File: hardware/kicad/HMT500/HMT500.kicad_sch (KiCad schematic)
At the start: 0 parts

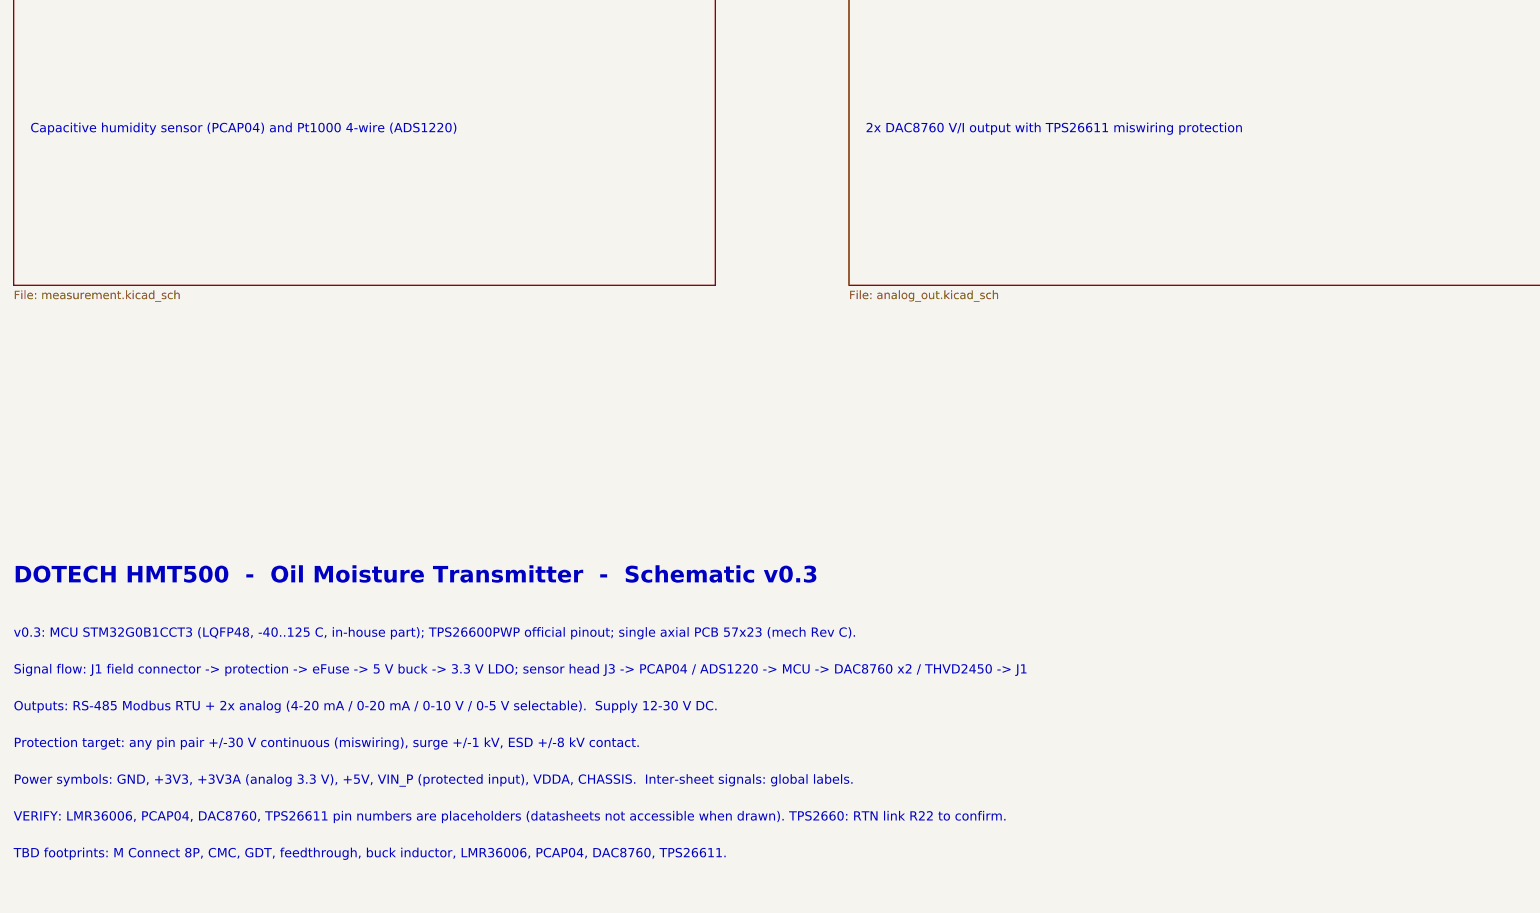
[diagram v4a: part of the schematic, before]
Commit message: Sensor harness W-1: JST SH 1.0 mm 4P between feedthrough and PCB J3
- Schematic v0.4: J3 = BM04B-SRSS-TB (top entry). Pins 1-2 MK33, 3-4 Pt1000
  2-wire with force/sense split at the J3 pads (68 nets, netlist check 0 errors)
- Parts list: J3 header, SHR-04V-S housing, SSH-003T-P0.2-H contacts, PTFE AWG30 wire
- Mech: J3 and harness in params/CAD/drawings (item 17, notes 5 and 9), PCAP04
  moved directly behind J3, PCB outline and KiCad board zone updated
- Test for harness clearance, J3 height and pin mapping
- Decision log #16; JST SH -25..+85 C rating added to open items

Co-Authored-By: Claude Opus 5.5 <noreply@anthropic.com>
Claude-Session: https://claude.ai/code/session_01JA2o8uJsqp9Vzsg4b665ev
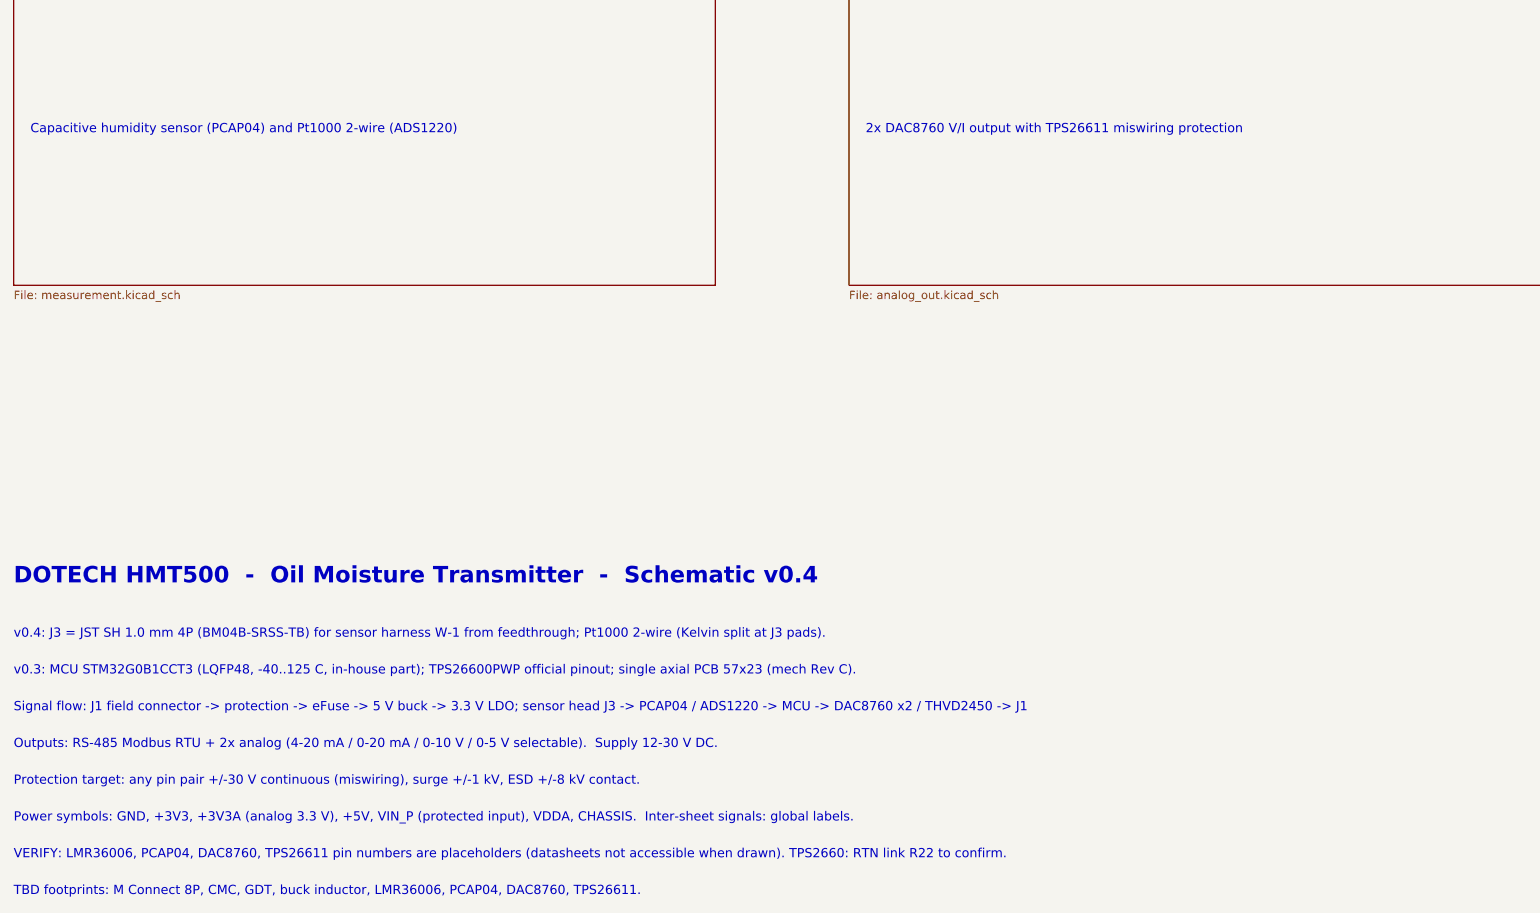
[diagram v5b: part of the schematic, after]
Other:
- note added: "Capacitive humidity sensor (PCAP04) and Pt1000 2-wire (ADS1220)"
- note added: "DOTECH HMT500 - Oil Moisture Transmitter - Schematic v0.4"
- note added: "TBD footprints: M Connect 8P, CMC, GDT, buck inductor, LMR36006, PCAP04, DAC8760, TPS26611."
- note added: "v0.4: J3 = JST SH 1.0 mm 4P (BM04B-SRSS-TB) for sensor harness W-1 from feedthrough; Pt1000 2-wire (Kelvin split at J3 pads)."
- note removed: "Capacitive humidity sensor (PCAP04) and Pt1000 4-wire (ADS1220)"
- note removed: "DOTECH HMT500 - Oil Moisture Transmitter - Schematic v0.3"
- note removed: "TBD footprints: M Connect 8P, CMC, GDT, feedthrough, buck inductor, LMR36006, PCAP04, DAC8760, TPS26611."
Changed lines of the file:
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@@
 (kicad_sch (version 20230121) (generator eeschema) (paper "A3")
-(title_block (title "HMT500  Top") (date "2026-09-26") (rev "0.3") (company "DOTECH Co., Ltd.") (comment 1 "Oil moisture transmitter HMT500 - RS-485 + 2x V/I analog output") (comment 2 "Design notes: docs/hw/circuit-design.md") (comment 3 "VERIFY=YES parts: pin numbers LMR36006/PCAP04/DAC8760/TPS26611; TPS2660 R22"))
+(title_block (title "HMT500  Top") (date "2026-09-29") (rev "0.4") (company "DOTECH Co., Ltd.") (comment 1 "Oil moisture transmitter HMT500 - RS-485 + 2x V/I analog output") (comment 2 "Design notes: docs/hw/circuit-design.md") (comment 3 "VERIFY=YES parts: pin numbers LMR36006/PCAP04/DAC8760/TPS26611; TPS2660 R22"))
 (sheet (at 30.48 55.88) (size 106.68 45.72) (fields_autoplaced) (stroke (width 0.1524) (type solid)) (fill (color 0 0 0 0.0000)) (property "Sheetname" "1. Connector & input protection" (at 30.48 55.118 0) (effects (font (size 1.8 1.8) bold) (justify left bottom))) (property "Sheetfile" "connector.kicad_sch" (at 30.48 102.362 0) (effects (font (size 1.27 1.27)) (justify left top))) (instances (project "HMT500" (path "/1ebb025b-11bd-5f7c-aaab-41e2a750e8b3" (page "2")))))
 (text "Field connector, 2-stage bidirectional TVS surge protection, chassis isolation" (at 33.02 78.74 0) (effects (font (size 1.4 1.4)) (justify left bottom)))
@@
 (text "STM32G0B1CCT3, SWD, status LED, fault pull-ups" (at 287.02 78.74 0) (effects (font (size 1.4 1.4)) (justify left bottom)))
 (sheet (at 30.48 132.08) (size 106.68 45.72) (fields_autoplaced) (stroke (width 0.1524) (type solid)) (fill (color 0 0 0 0.0000)) (property "Sheetname" "4. Measurement" (at 30.48 131.318 0) (effects (font (size 1.8 1.8) bold) (justify left bottom))) (property "Sheetfile" "measurement.kicad_sch" (at 30.48 178.562 0) (effects (font (size 1.27 1.27)) (justify left top))) (instances (project "HMT500" (path "/1ebb025b-11bd-5f7c-aaab-41e2a750e8b3" (page "5")))))
-(text "Capacitive humidity sensor (PCAP04) and Pt1000 4-wire (ADS1220)" (at 33.02 154.94 0) (effects (font (size 1.4 1.4)) (justify left bottom)))
+(text "Capacitive humidity sensor (PCAP04) and Pt1000 2-wire (ADS1220)" (at 33.02 154.94 0) (effects (font (size 1.4 1.4)) (justify left bottom)))
 (sheet (at 157.48 132.08) (size 106.68 45.72) (fields_autoplaced) (stroke (width 0.1524) (type solid)) (fill (color 0 0 0 0.0000)) (property "Sheetname" "5. Analog outputs" (at 157.48 131.318 0) (effects (font (size 1.8 1.8) bold) (justify left bottom))) (property "Sheetfile" "analog_out.kicad_sch" (at 157.48 178.562 0) (effects (font (size 1.27 1.27)) (justify left top))) (instances (project "HMT500" (path "/1ebb025b-11bd-5f7c-aaab-41e2a750e8b3" (page "6")))))
 (text "2x DAC8760 V/I output with TPS26611 miswiring protection" (at 160.02 154.94 0) (effects (font (size 1.4 1.4)) (justify left bottom)))
 (sheet (at 284.48 132.08) (size 106.68 45.72) (fields_autoplaced) (stroke (width 0.1524) (type solid)) (fill (color 0 0 0 0.0000)) (property "Sheetname" "6. RS-485" (at 284.48 131.318 0) (effects (font (size 1.8 1.8) bold) (justify left bottom))) (property "Sheetfile" "rs485.kicad_sch" (at 284.48 178.562 0) (effects (font (size 1.27 1.27)) (justify left top))) (instances (project "HMT500" (path "/1ebb025b-11bd-5f7c-aaab-41e2a750e8b3" (page "7")))))
 (text "THVD2450 +/-70V fault-protected transceiver" (at 287.02 154.94 0) (effects (font (size 1.4 1.4)) (justify left bottom)))
-(text "DOTECH HMT500  -  Oil Moisture Transmitter  -  Schematic v0.3" (at 30.48 223.52 0) (effects (font (size 2.5 2.5) bold) (justify left bottom)))
-(text "v0.3: MCU STM32G0B1CCT3 (LQFP48, -40..125 C, in-house part); TPS26600PWP official pinout; single axial PCB 57x23 (mech Rev C)." (at 30.48 231.648 0) (effects (font (size 1.4 1.4)) (justify left bottom)))
-(text "Signal flow: J1 field connector -> protection -> eFuse -> 5 V buck -> 3.3 V LDO; sensor head J3 -> PCAP04 / ADS1220 -> MCU -> DAC8760 x2 / THVD2450 -> J1" (at 30.48 237.236 0) (effects (font (size 1.4 1.4)) (justify left bottom)))
-(text "Outputs: RS-485 Modbus RTU + 2x analog (4-20 mA / 0-20 mA / 0-10 V / 0-5 V selectable).  Supply 12-30 V DC." (at 30.48 242.824 0) (effects (font (size 1.4 1.4)) (justify left bottom)))
-(text "Protection target: any pin pair +/-30 V continuous (miswiring), surge +/-1 kV, ESD +/-8 kV contact." (at 30.48 248.412 0) (effects (font (size 1.4 1.4)) (justify left bottom)))
-(text "Power symbols: GND, +3V3, +3V3A (analog 3.3 V), +5V, VIN_P (protected input), VDDA, CHASSIS.  Inter-sheet signals: global labels." (at 30.48 254 0) (effects (font (size 1.4 1.4)) (justify left bottom)))
-(text "VERIFY: LMR36006, PCAP04, DAC8760, TPS26611 pin numbers are placeholders (datasheets not accessible when drawn). TPS2660: RTN link R22 to confirm." (at 30.48 259.588 0) (effects (font (size 1.4 1.4)) (justify left bottom)))
-(text "TBD footprints: M Connect 8P, CMC, GDT, feedthrough, buck inductor, LMR36006, PCAP04, DAC8760, TPS26611." (at 30.48 265.176 0) (effects (font (size 1.4 1.4)) (justify left bottom)))
+(text "DOTECH HMT500  -  Oil Moisture Transmitter  -  Schematic v0.4" (at 30.48 223.52 0) (effects (font (size 2.5 2.5) bold) (justify left bottom)))
+(text "v0.4: J3 = JST SH 1.0 mm 4P (BM04B-SRSS-TB) for sensor harness W-1 from feedthrough; Pt1000 2-wire (Kelvin split at J3 pads)." (at 30.48 231.648 0) (effects (font (size 1.4 1.4)) (justify left bottom)))
+(text "v0.3: MCU STM32G0B1CCT3 (LQFP48, -40..125 C, in-house part); TPS26600PWP official pinout; single axial PCB 57x23 (mech Rev C)." (at 30.48 237.236 0) (effects (font (size 1.4 1.4)) (justify left bottom)))
+(text "Signal flow: J1 field connector -> protection -> eFuse -> 5 V buck -> 3.3 V LDO; sensor head J3 -> PCAP04 / ADS1220 -> MCU -> DAC8760 x2 / THVD2450 -> J1" (at 30.48 242.824 0) (effects (font (size 1.4 1.4)) (justify left bottom)))
+(text "Outputs: RS-485 Modbus RTU + 2x analog (4-20 mA / 0-20 mA / 0-10 V / 0-5 V selectable).  Supply 12-30 V DC." (at 30.48 248.412 0) (effects (font (size 1.4 1.4)) (justify left bottom)))
+(text "Protection target: any pin pair +/-30 V continuous (miswiring), surge +/-1 kV, ESD +/-8 kV contact." (at 30.48 254 0) (effects (font (size 1.4 1.4)) (justify left bottom)))
+(text "Power symbols: GND, +3V3, +3V3A (analog 3.3 V), +5V, VIN_P (protected input), VDDA, CHASSIS.  Inter-sheet signals: global labels." (at 30.48 259.588 0) (effects (font (size 1.4 1.4)) (justify left bottom)))
+(text "VERIFY: LMR36006, PCAP04, DAC8760, TPS26611 pin numbers are placeholders (datasheets not accessible when drawn). TPS2660: RTN link R22 to confirm." (at 30.48 265.176 0) (effects (font (size 1.4 1.4)) (justify left bottom)))
+(text "TBD footprints: M Connect 8P, CMC, GDT, buck inductor, LMR36006, PCAP04, DAC8760, TPS26611." (at 30.48 270.764 0) (effects (font (size 1.4 1.4)) (justify left bottom)))
 (sheet_instances (path "/" (page "1")))
 )

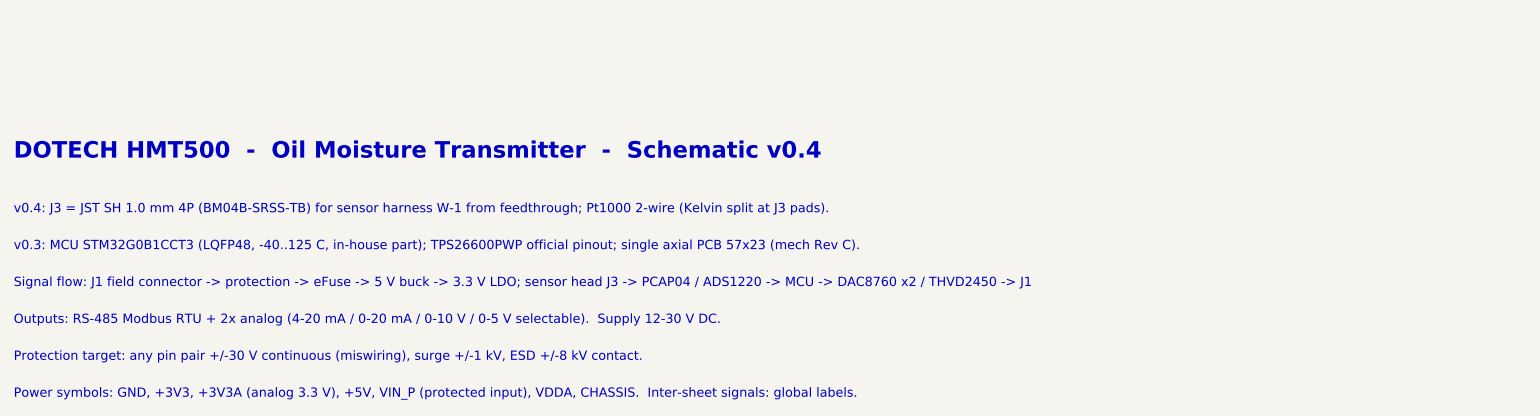
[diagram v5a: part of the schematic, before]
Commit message: HMT500 mech Rev F: DOTECH oil filter cap, no feedthrough
- Cap replaced by DOTECH SUS probe oil filter 390000-001100 (from the
  2020-06-08 DWG): SUS304, 12 x 32, M10x1.0 x 8.5, 20 side holes 3 mm, tip 3 mm.
  Exposed probe 48, overall 158. Probe plug 8.5 -> 7.6 to fit the 8 mm bore
- Feedthrough removed: 7 mm channel runs through to the rear counterbore and
  carries only harness W-1 (HTX99R rear pins -> J3, 60 mm). Rear pins potted (item 5)
- Drawings, CAD, renders, HTX99R-SC notes, RFQ, docs and tests updated
- Decision log #17; open items: HTX99R thread pitch (1.0 vs 0.75), HTX99R as
  pressure barrier, SUS304 filter material
- Filter DWG added to hardware/mech/ref

Co-Authored-By: Claude Opus 5.5 <noreply@anthropic.com>
Claude-Session: https://claude.ai/code/session_01JA2o8uJsqp9Vzsg4b665ev
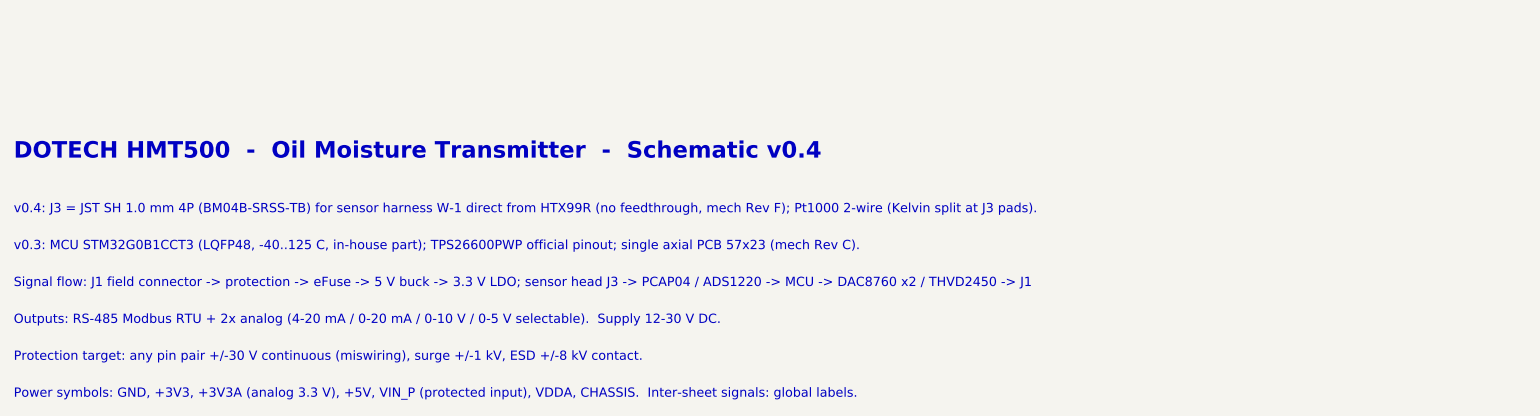
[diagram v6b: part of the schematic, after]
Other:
- note added: "v0.4: J3 = JST SH 1.0 mm 4P (BM04B-SRSS-TB) for sensor harness W-1 direct from HTX99R (no feedthrough, mech Rev F); Pt1000 2-wire (Kelvin split at J3 pads)."
- note removed: "v0.4: J3 = JST SH 1.0 mm 4P (BM04B-SRSS-TB) for sensor harness W-1 from feedthrough; Pt1000 2-wire (Kelvin split at J3 pads)."
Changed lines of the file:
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@@
 (text "THVD2450 +/-70V fault-protected transceiver" (at 287.02 154.94 0) (effects (font (size 1.4 1.4)) (justify left bottom)))
 (text "DOTECH HMT500  -  Oil Moisture Transmitter  -  Schematic v0.4" (at 30.48 223.52 0) (effects (font (size 2.5 2.5) bold) (justify left bottom)))
-(text "v0.4: J3 = JST SH 1.0 mm 4P (BM04B-SRSS-TB) for sensor harness W-1 from feedthrough; Pt1000 2-wire (Kelvin split at J3 pads)." (at 30.48 231.648 0) (effects (font (size 1.4 1.4)) (justify left bottom)))
+(text "v0.4: J3 = JST SH 1.0 mm 4P (BM04B-SRSS-TB) for sensor harness W-1 direct from HTX99R (no feedthrough, mech Rev F); Pt1000 2-wire (Kelvin split at J3 pads)." (at 30.48 231.648 0) (effects (font (size 1.4 1.4)) (justify left bottom)))
 (text "v0.3: MCU STM32G0B1CCT3 (LQFP48, -40..125 C, in-house part); TPS26600PWP official pinout; single axial PCB 57x23 (mech Rev C)." (at 30.48 237.236 0) (effects (font (size 1.4 1.4)) (justify left bottom)))
 (text "Signal flow: J1 field connector -> protection -> eFuse -> 5 V buck -> 3.3 V LDO; sensor head J3 -> PCAP04 / ADS1220 -> MCU -> DAC8760 x2 / THVD2450 -> J1" (at 30.48 242.824 0) (effects (font (size 1.4 1.4)) (justify left bottom)))
